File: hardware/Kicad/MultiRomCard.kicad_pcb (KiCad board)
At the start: 2 copper layers, 160 x 100 mm, 9 parts, among them P1 VC4000_Cartridge_Bus, U1 Arduino_UNO, U2 74HC595, U3 74HC595, U4 74HC595, U5 6264, U6 74HC245, U7 74HC245, U8 74HC245

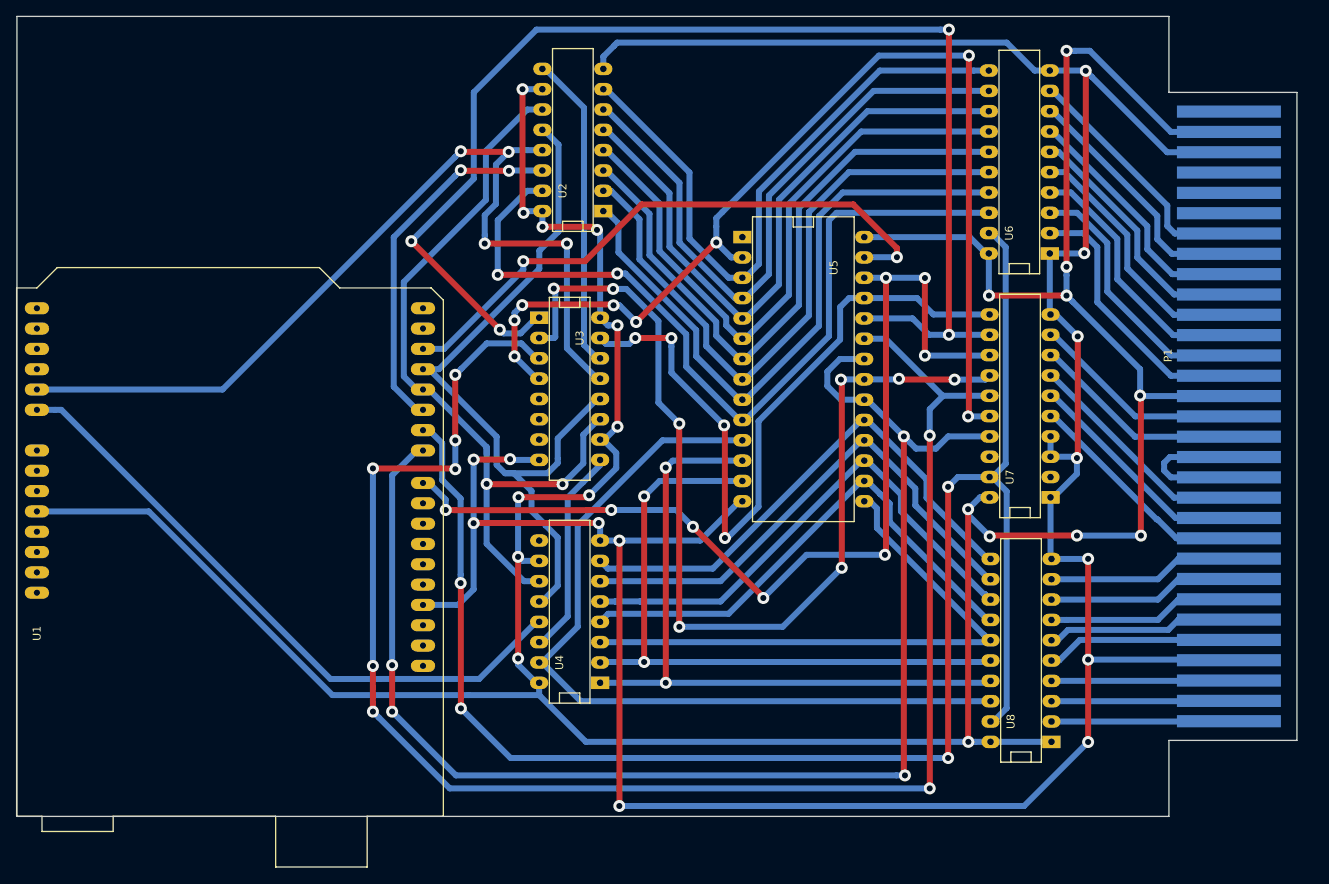
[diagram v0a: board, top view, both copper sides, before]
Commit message: [PCB] Add ground copper zone; minor reroutings.
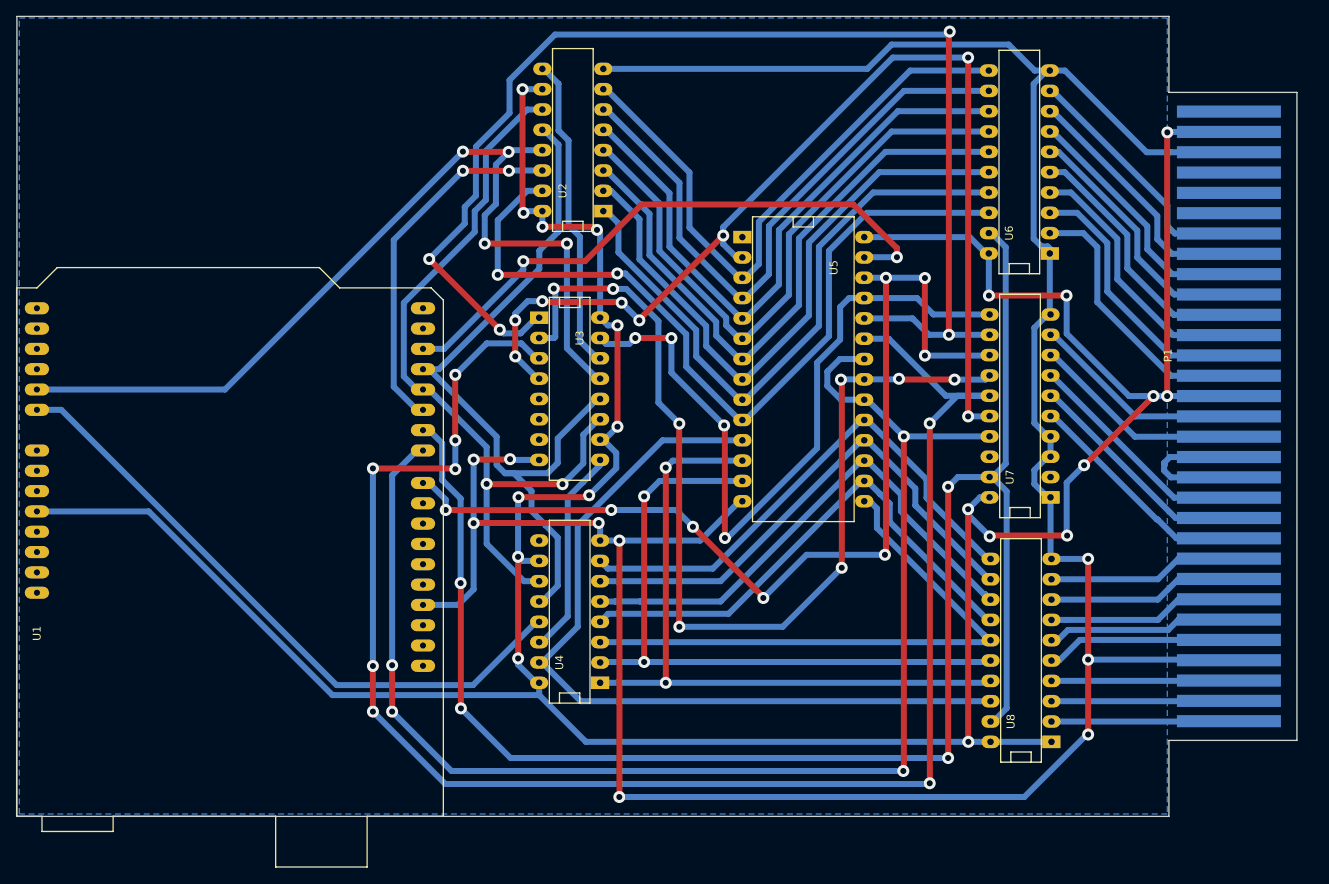
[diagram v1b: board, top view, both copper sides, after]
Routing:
- net VCC: track 432.1 -> 415.9 mm
- net GND: track 371.0 -> 361.6 mm, vias 13 -> 9
- net /A11: track 207.4 -> 211.3 mm
- net /A9: track 160.7 -> 156.9 mm
- net /A7: track 78.8 -> 75.8 mm
- net /A6: track 78.8 -> 76.3 mm
- net CE1SRAM: track 175.7 -> 173.5 mm
- net /A5: track 78.8 -> 76.6 mm
- net /A4: track 79.4 -> 77.2 mm
- net /A2: track 80.7 -> 78.4 mm
- net /A1: track 80.8 -> 78.5 mm
- net /A0: track 104.5 -> 102.3 mm
- net /A3: track 79.9 -> 77.6 mm
- net /A12: track 135.4 -> 134.4 mm
- net Net-(U1-Pad5): track 96.8 -> 95.9 mm
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- added copper zone on B.Cu, net GND

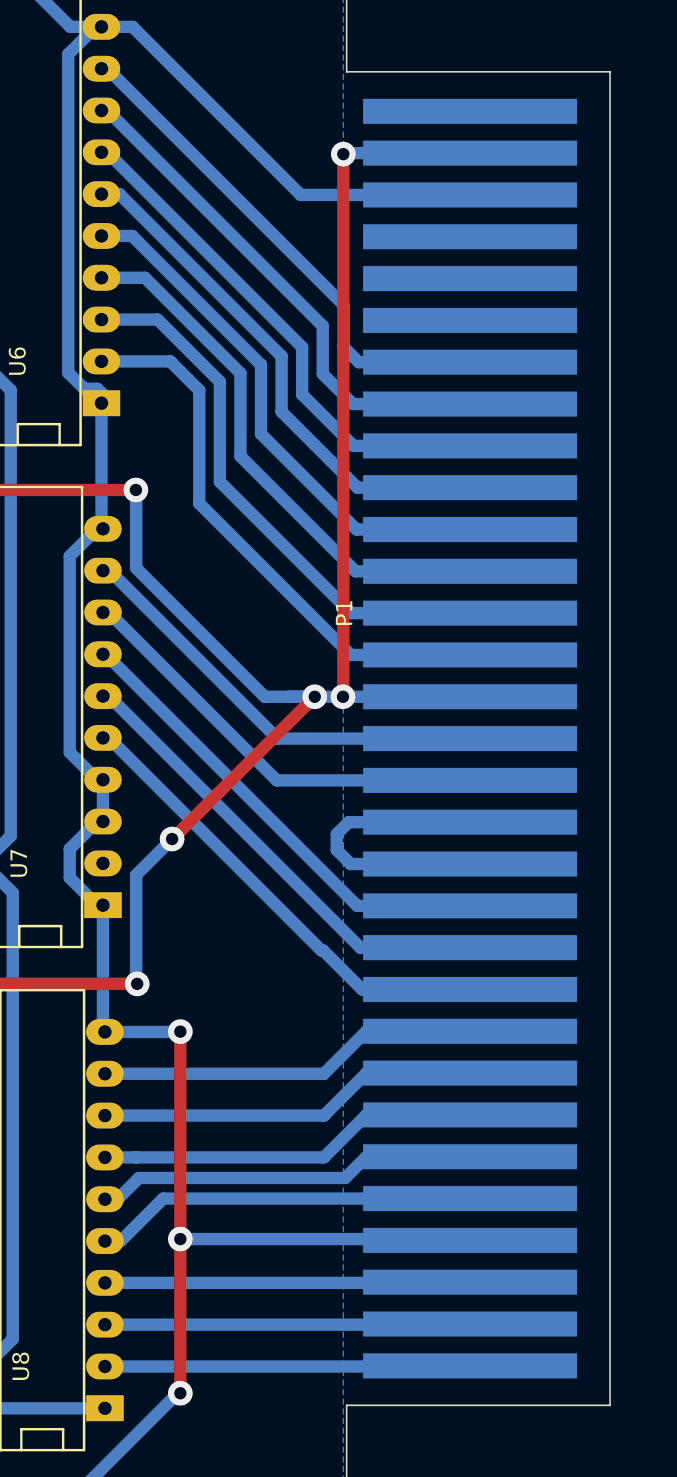
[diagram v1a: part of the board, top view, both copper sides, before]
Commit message: [PCB] Make Cartridge Bus Pins 1mm longer.
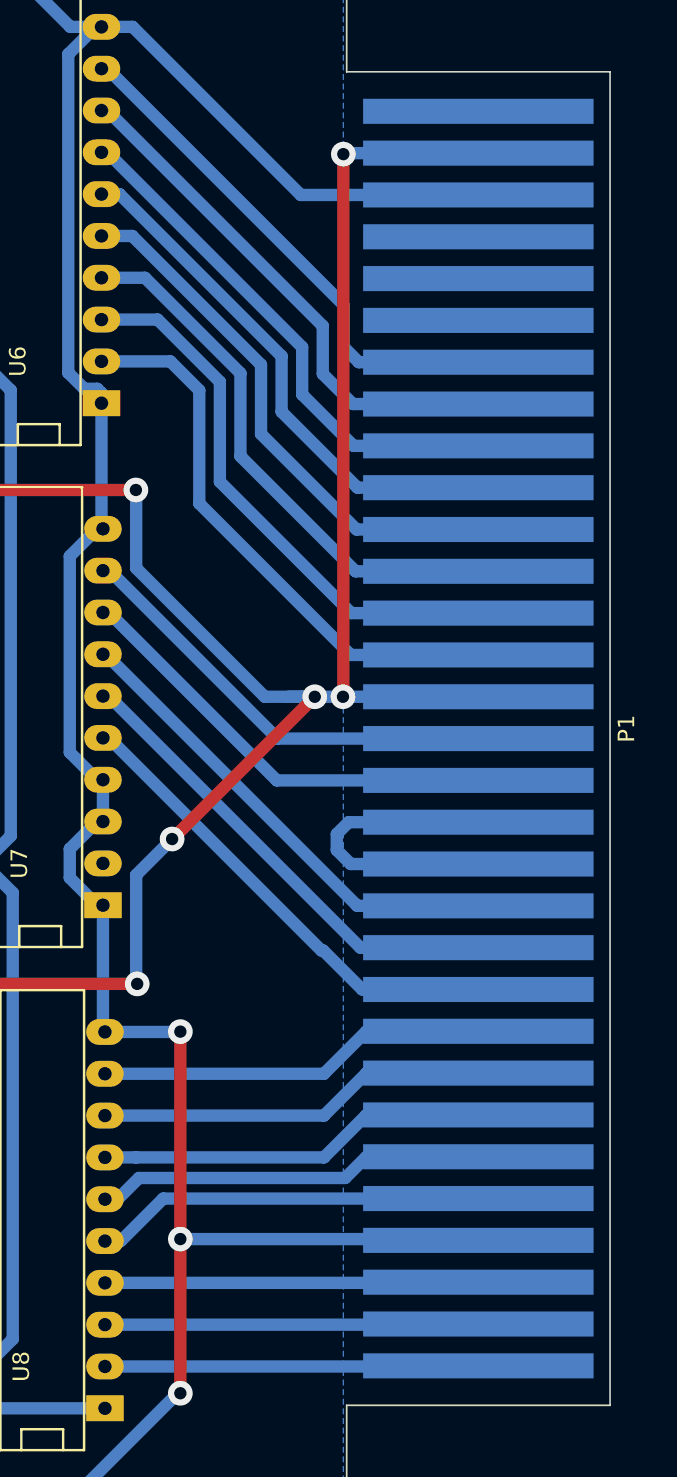
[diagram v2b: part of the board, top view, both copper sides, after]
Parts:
- P1: footprint VC4000_CartridgeBus -> VC4000_MultiRom:VC4000_CartridgeBus
- moved P1 0.50 mm to (218.0, 98.5)
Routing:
- net Net-(P1-Pad13): track 17.8 -> 18.8 mm
- net GND: track 361.6 -> 362.1 mm
- net /ED3: track 23.2 -> 23.7 mm
- net VCC: track 415.9 -> 416.4 mm
- net Net-(P1-Pad12): track 28.6 -> 29.1 mm
- net /ED7: track 23.2 -> 23.7 mm
- net /ED6: track 23.2 -> 23.7 mm
- net /ED5: track 23.2 -> 23.7 mm
- net /ED4: track 23.2 -> 23.7 mm
- net /ED2: track 22.2 -> 22.7 mm
- net /ED1: track 22.2 -> 22.7 mm
- net /ED0: track 22.2 -> 22.7 mm
- net /EA9: track 26.5 -> 27.0 mm
- net /EA8: track 26.5 -> 27.0 mm
- net /EA7: track 31.3 -> 31.8 mm
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
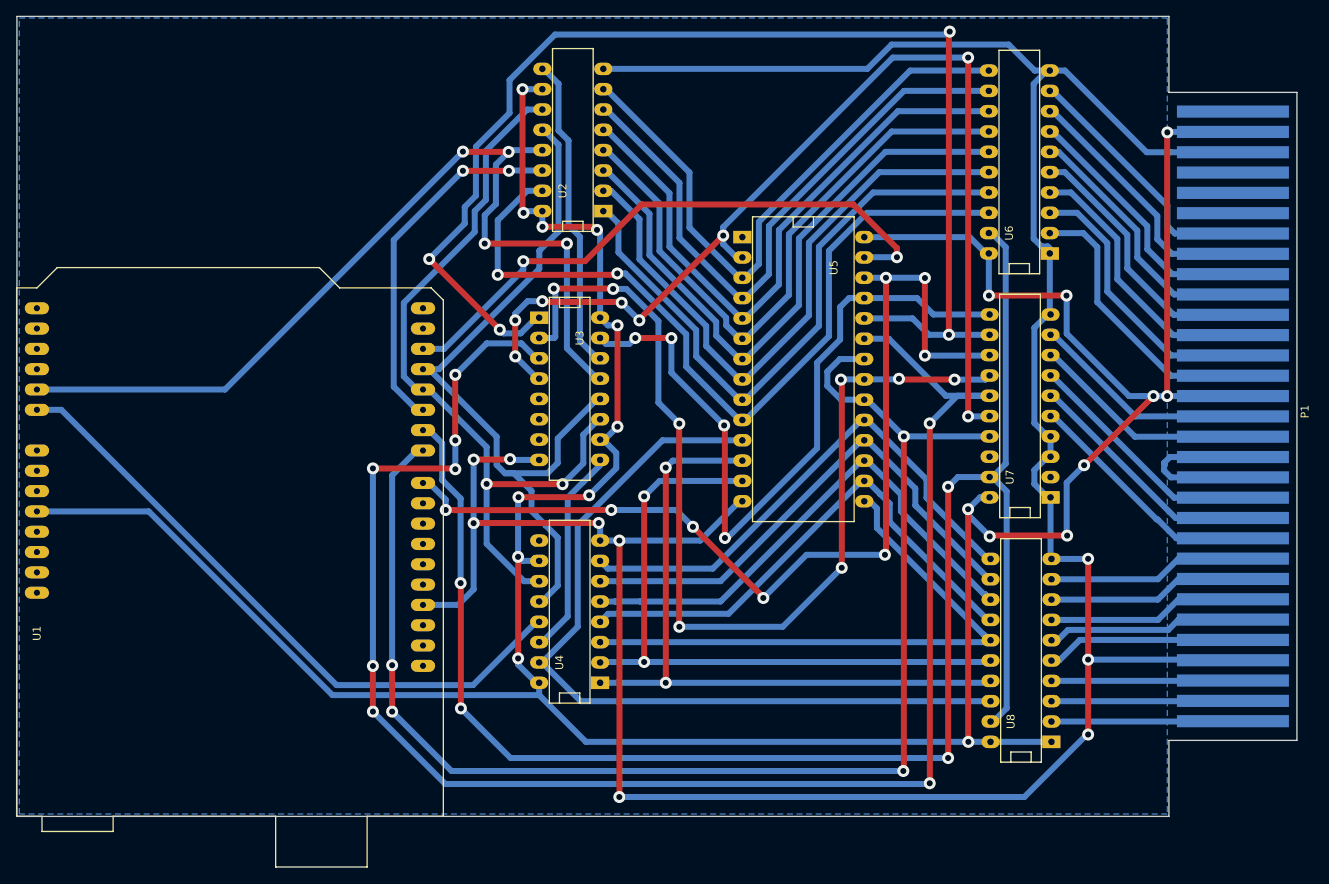
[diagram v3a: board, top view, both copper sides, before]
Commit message: [SCH/PCB] Added IC power decoupling caps.
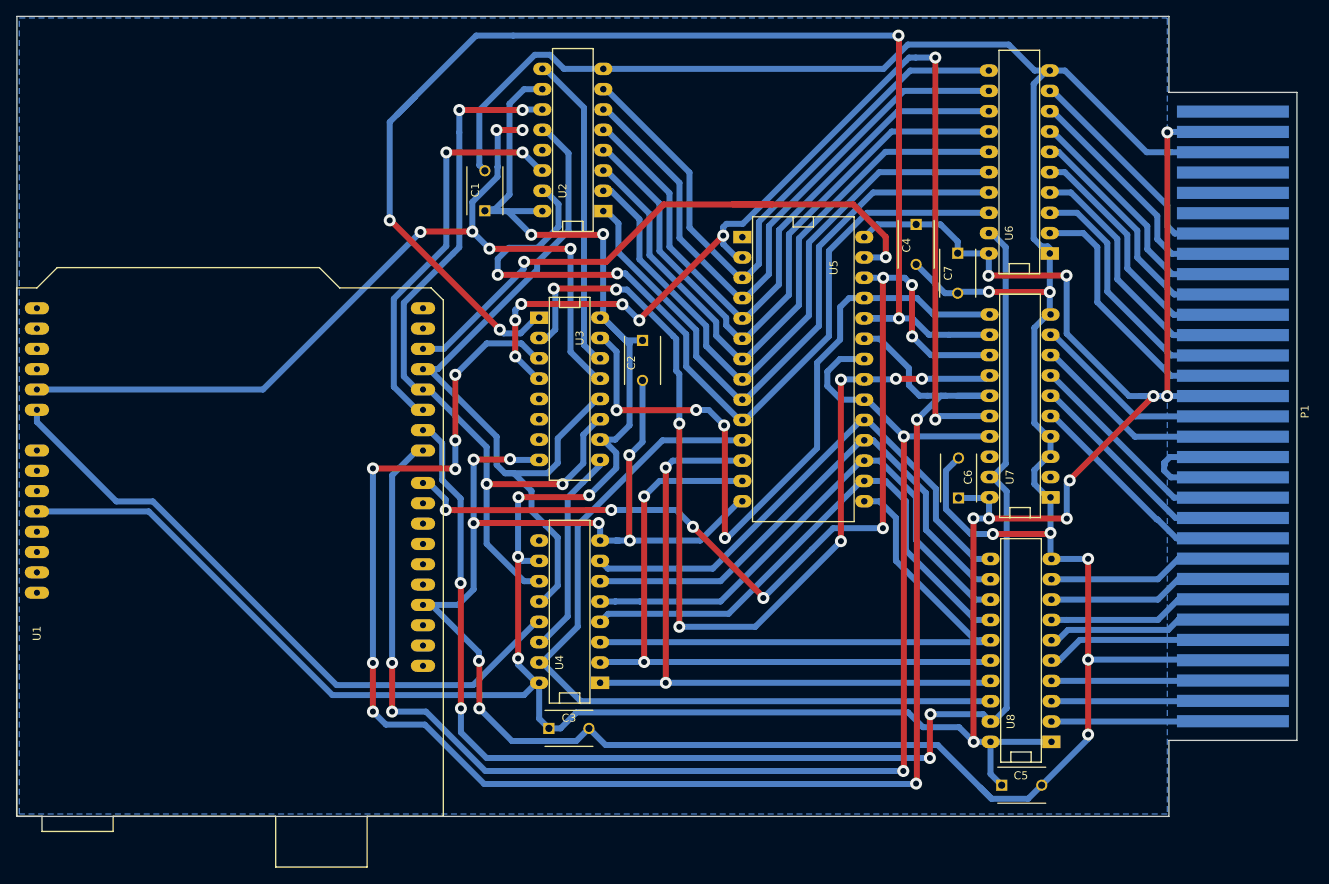
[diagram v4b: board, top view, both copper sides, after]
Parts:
- added C1: .1uF, Capacitors_ThroughHole:C_Disc_D6_P5, F.Cu at (124.5, 72.8)
- added C2: .1uF, Capacitors_ThroughHole:C_Disc_D6_P5, F.Cu at (144.2, 89.0)
- added C3: .1uF, Capacitors_ThroughHole:C_Disc_D6_P5, F.Cu at (132.5, 137.5)
- added C4: .1uF, Capacitors_ThroughHole:C_Disc_D6_P5, F.Cu at (178.4, 74.5)
- added C5: .1uF, Capacitors_ThroughHole:C_Disc_D6_P5, F.Cu at (189.1, 144.6)
- added C6: .1uF, Capacitors_ThroughHole:C_Disc_D6_P5, F.Cu at (183.7, 108.7)
- added C7: .1uF, Capacitors_ThroughHole:C_Disc_D6_P5, F.Cu at (183.6, 78.1)
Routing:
- net GND: track 362.1 -> 460.1 mm, vias 9 -> 15
- net VCC: track 416.4 -> 445.5 mm, vias 20 -> 16
- net OEVCBUS: track 205.2 -> 178.7 mm
- net /A9: track 156.9 -> 165.1 mm
- net Net-(U1-Pad28): track 117.4 -> 111.5 mm, vias 4 -> 6
- net Net-(U1-Pad5): track 95.9 -> 100.9 mm, vias 2 -> 4
- net Net-(U1-Pad6): track 45.4 -> 49.8 mm
- net CE2SRAM: track 126.9 -> 122.7 mm
- net /A0: track 102.3 -> 105.2 mm
- net /D3: track 73.3 -> 76.2 mm
- net WESRAM: track 74.8 -> 77.7 mm
- net /D4: track 64.6 -> 67.3 mm
- net /A10: track 128.1 -> 125.5 mm
- net /D5: track 64.5 -> 66.5 mm
- net /D6: track 64.5 -> 66.0 mm
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
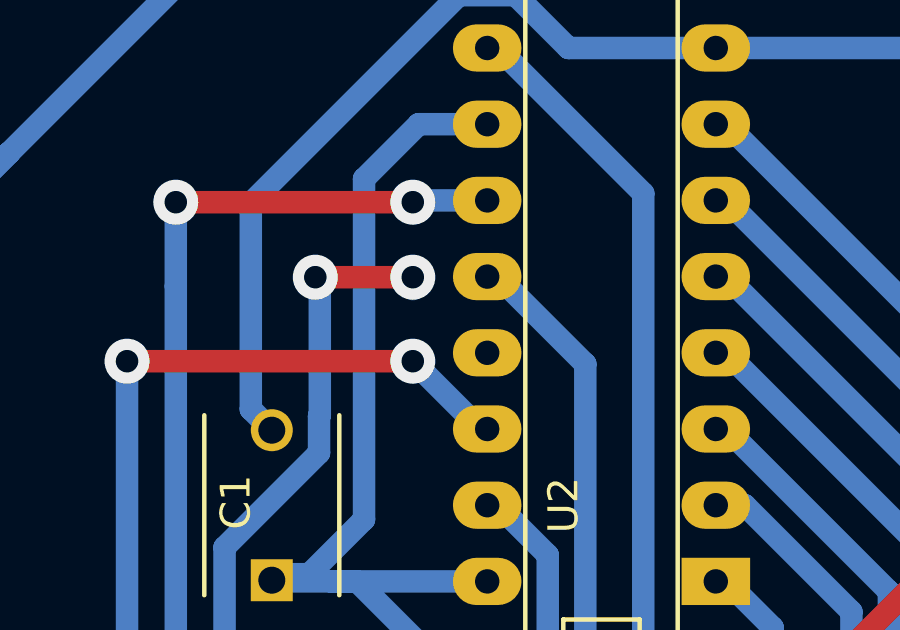
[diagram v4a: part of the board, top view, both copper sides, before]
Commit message: [PCB] Added missing last connection.
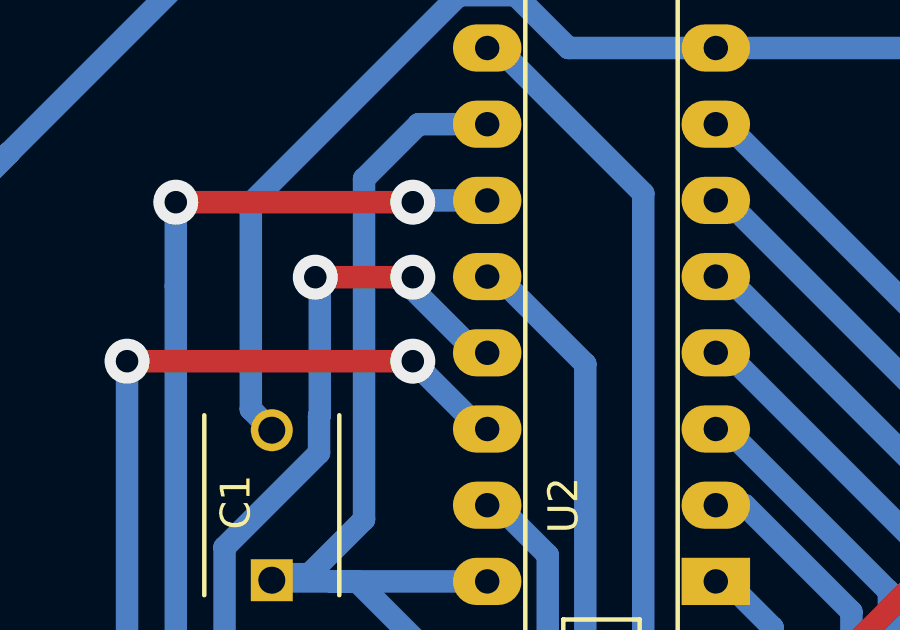
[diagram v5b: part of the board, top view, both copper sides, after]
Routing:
- net Net-(U1-Pad28): track 111.5 -> 114.8 mm
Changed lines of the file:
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@@
     (thickness 1.6)
     (drawings 8)
-    (tracks 849)
+    (tracks 851)
     (zones 0)
     (modules 16)
@@
   (via (at 174.6 78.6) (size 1.5) (drill 0.75) (layers F.Cu B.Cu) (net 41))
   (segment (start 171.95 78.6) (end 171.92 78.63) (width 0.75) (layer B.Cu) (net 41) (status 30))
+  (segment (start 129.200031 62.7) (end 129.200031 63.095631) (width 0.75) (layer B.Cu) (net 48))
+  (segment (start 129.200031 63.095631) (end 131.3244 65.22) (width 0.75) (layer B.Cu) (net 48))
+  (segment (start 131.3244 65.22) (end 131.68 65.22) (width 0.75) (layer B.Cu) (net 48))
   (segment (start 116.449056 75.450944) (end 96.76 95.14) (width 0.75) (layer B.Cu) (net 48))
   (segment (start 96.76 95.14) (end 68.5 95.14) (width 0.75) (layer B.Cu) (net 48))
@@
   (segment (start 126.075001 67.324999) (end 126.1 67.3) (width 0.75) (layer B.Cu) (net 48))
   (via (at 129.200031 62.7) (size 1.5) (drill 0.75) (layers F.Cu B.Cu) (net 48))
-  (segment (start 129.200031 63.095631) (end 129.200031 62.7) (width 0.75) (layer B.Cu) (net 48))
   (segment (start 135.2 77.54998) (end 125.078651 77.54998) (width 0.75) (layer F.Cu) (net 48))
   (segment (start 125.078651 77.54998) (end 125.06528 77.536609) (width 0.75) (layer F.Cu) (net 48))
